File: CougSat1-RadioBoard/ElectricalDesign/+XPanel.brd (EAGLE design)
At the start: 79 x 90 mm, 64 parts, among them J1 ADCS Connector, J2 Low Gain +, J3 Low Gain -, J4 Low Gain Coax, J5 GPS Coax, J6 EPS Connector, U1 AD8515, U3 AD7291

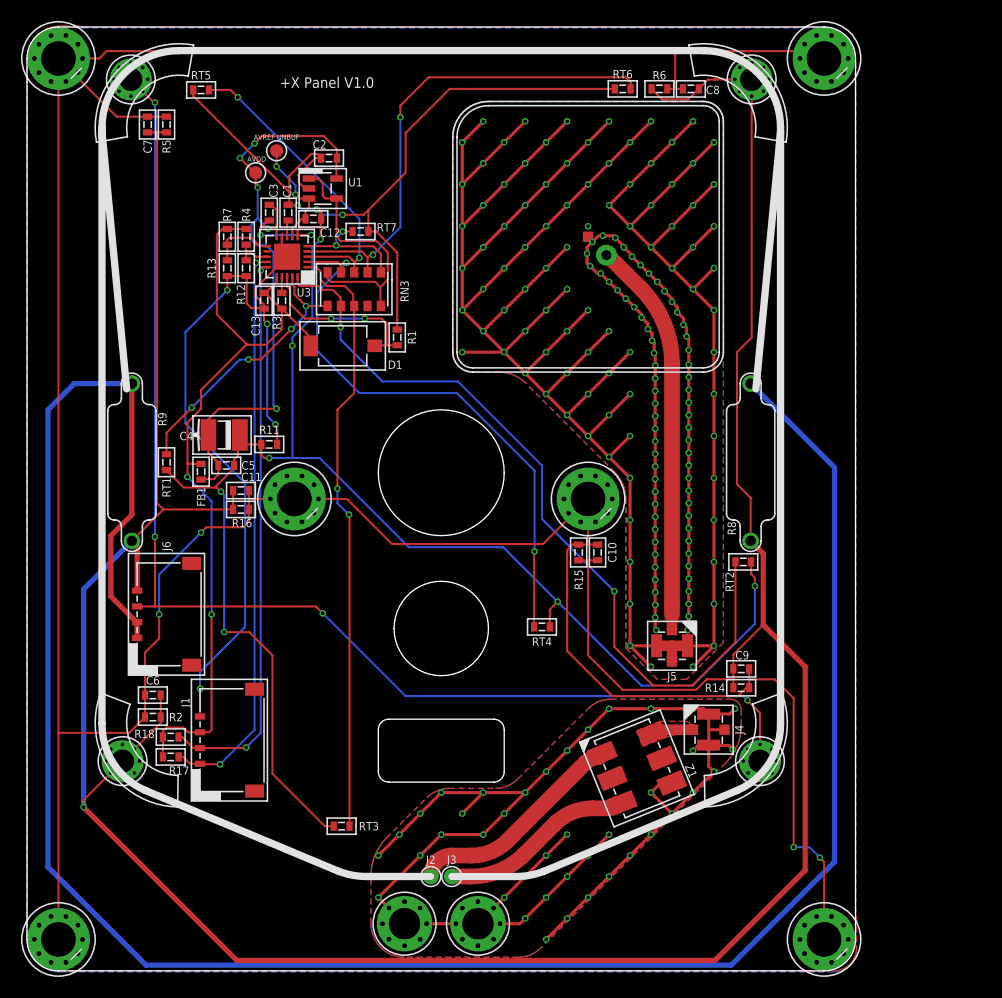
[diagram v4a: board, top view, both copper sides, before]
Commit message: Created mCAD and updated board reference designators and RF soldermask
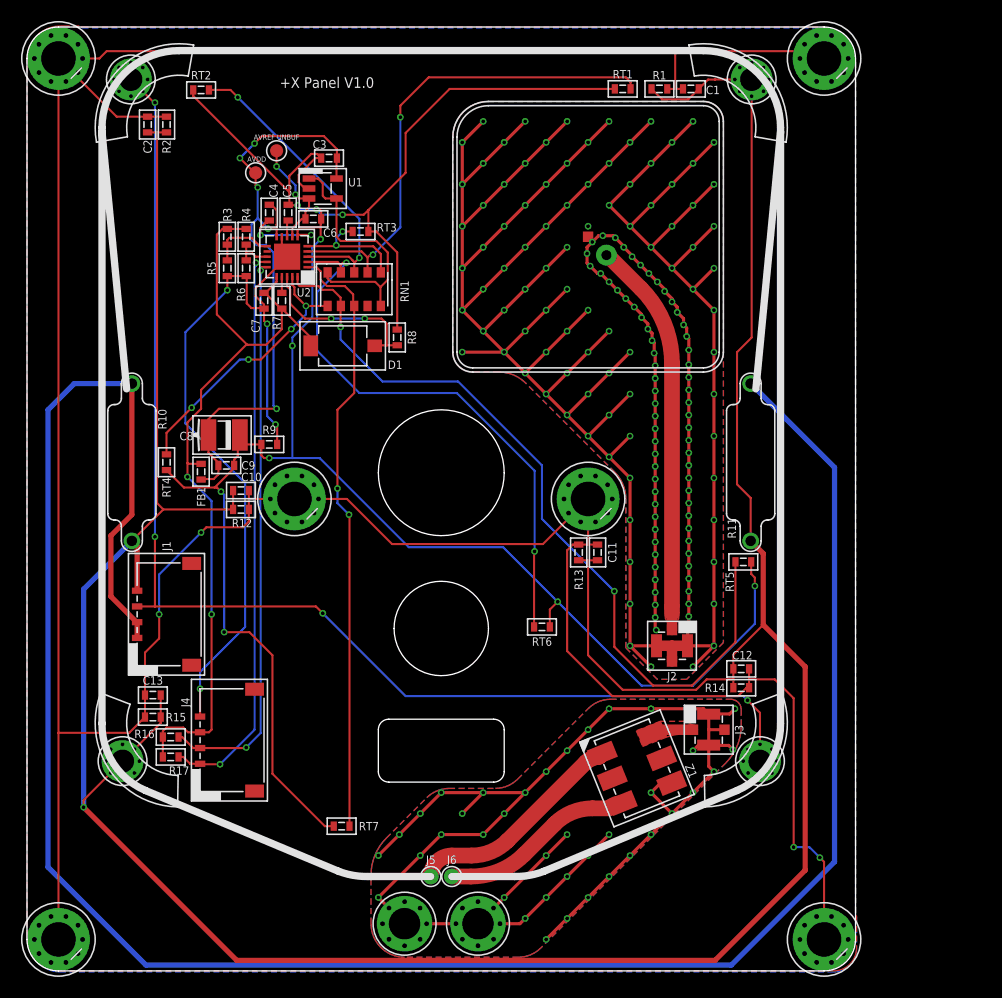
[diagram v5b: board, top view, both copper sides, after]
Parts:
- removed R18: 10kΩ 0.1%, CougsInSpace-Resistors:1608
- added R10: 15Ω 5%, CougsInSpace-Resistors:THT-15MM
- C1: value 1µF 10% -> 100nF 10%
- C12: value 10µF 10% -> 100nF 10%
- C4: value 4.7µF 10% -> 100nF 10%; device CougsInSpace-Capacitors:4028-POL -> CougsInSpace-Capacitors:1608
- C5: value 100nF 10% -> 1µF 10%
- C6: value 100nF 10% -> 10µF 10%
- C8: value 100nF 10% -> 4.7µF 10%; device CougsInSpace-Capacitors:1608 -> CougsInSpace-Capacitors:4028-POL
- H1, H2: value M2 -> M3; device CougsInSpace-Hardware:MOUNTING_HOLE-2.2 -> CougsInSpace-Hardware:MOUNTING_HOLE-3.3
- H10, H9: value M3 -> M2 Nut - 1mm; device CougsInSpace-Hardware:MOUNTING_HOLE-3.3 -> CougsInSpace-Hardware:MOUNTING_HOLE-M2_NUT
- H11, H12: value M2 Nut - 1mm -> M3; device CougsInSpace-Hardware:MOUNTING_HOLE-M2_NUT -> CougsInSpace-Hardware:MOUNTING_HOLE-3.3
- H7, H8: value M3 -> M2; device CougsInSpace-Hardware:MOUNTING_HOLE-3.3 -> CougsInSpace-Hardware:MOUNTING_HOLE-2.2
- J1: value ADCS Connector -> EPS Connector
- J2: value Low Gain + -> GPS Coax; device CougsInSpace-Connectors:THT-0.7 -> CougsInSpace-Connectors:U.FL
- J3: value Low Gain - -> Low Gain Coax; device CougsInSpace-Connectors:THT-0.7 -> CougsInSpace-Connectors:U.FL
- J4: value Low Gain Coax -> ADCS Connector; device CougsInSpace-Connectors:U.FL -> CougsInSpace-Connectors:PICOLOCK1.5-04
- J5: value GPS Coax -> Low Gain +; device CougsInSpace-Connectors:U.FL -> CougsInSpace-Connectors:THT-0.7
- J6: value EPS Connector -> Low Gain -; device CougsInSpace-Connectors:PICOLOCK1.5-04 -> CougsInSpace-Connectors:THT-0.7
- R1: value 2kΩ 0.1% -> 0Ω <20mΩ
- R11: value 0Ω <20mΩ -> 15Ω 5%; device CougsInSpace-Resistors:1608 -> CougsInSpace-Resistors:THT-15MM
- R16: value 0Ω <20mΩ -> 10kΩ 0.1%
- R3: value 1kΩ 0.1% -> 0Ω <20mΩ
- R7: value 0Ω <20mΩ -> 1kΩ 0.1%
- R8: value 15Ω 5% -> 2kΩ 0.1%; device CougsInSpace-Resistors:THT-15MM -> CougsInSpace-Resistors:1608
- R9: value 15Ω 5% -> 0Ω <20mΩ; device CougsInSpace-Resistors:THT-15MM -> CougsInSpace-Resistors:1608
- moved H1 94.7 mm to (-36.5, 42.0)
- moved H7 94.7 mm to (-30.4, -25.0)
- moved RT2 68.5 mm to (-22.9, 39.0), turned to 0 degrees
- moved RT5 68.5 mm to (28.8, -6.00), turned to 180 degrees
- moved H2 66.1 mm to (36.5, 42.0)
- moved H6 65.7 mm to (14.0, 0.00)
- moved H3 65.0 mm to (-29.6, 40.0)
- moved C12 59.2 mm to (28.6, -16.2), turned to 180 degrees
- moved RT3 56.7 mm to (-7.70, 25.5), turned to 180 degrees
- moved RT7 56.7 mm to (-9.50, -31.2), turned to 0 degrees
- moved R2 56.5 mm to (-26.2, 35.7), turned to 90 degrees
- moved RT1 56.2 mm to (17.3, 39.1), turned to 0 degrees
- moved C8 55.4 mm to (-20.7, 6.10), turned to 180 degrees
- moved C9 52.8 mm to (-20.5, 3.20), turned to 0 degrees
- moved RT6 51.9 mm to (9.60, -12.2), turned to 180 degrees
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- renumbered RN3 to RN1, U3 to U2
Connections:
- net 3.3V: now also C7.1, J4.3, R16.2; no longer C13.1, J1.3, R18.2
- net ADC_AS0: now also R3.1, R5.2; no longer R13.2, R7.1
- net ADC_AS1: now also R6.2; no longer R12.2
- net AGND: now also C4.2, C6.2, C8.C, C9.2, R8.1, R9.1; no longer C1.2, C12.2, C2.2, C4.C, R1.1, R11.1
- net AVDD: now also C4.1, C8.A, C9.1; no longer C2.1, C4.A, C5.1
- net AVREF_UNBUF: now also C6.1; no longer C12.1
- net CHASSIS: now also C1.1, C12.1, C13.1, C2.1, H1.1, H1.V1, H1.V10, H1.V2, H1.V3, H1.V4, H1.V5, H1.V6, H1.V7, H1.V8, H1.V9, H11.1, H11.V1, H11.V10, H11.V2, H11.V3, H11.V4, H11.V5, H11.V6, H11.V7, H11.V8, H11.V9, H12.1, H12.V1, H12.V10, H12.V2, H12.V3, H12.V4, H12.V5, H12.V6, H12.V7, H12.V8, H12.V9, H2.1, H2.V1, H2.V10, H2.V2, H2.V3, H2.V4, H2.V5, H2.V6, H2.V7, H2.V8, H2.V9, R1.2, R12.2, R13.2; no longer C6.1, C7.1, C8.1, C9.1, H10.1, H10.V1, H10.V10, H10.V2, H10.V3, H10.V4, H10.V5, H10.V6, H10.V7, H10.V8, H10.V9, H7.1, H7.V1, H7.V10, H7.V2, H7.V3, H7.V4, H7.V5, H7.V6, H7.V7, H7.V8, H7.V9, H8.1, H8.V1, H8.V10, H8.V2, H8.V3, H8.V4, H8.V5, H8.V6, H8.V7, H8.V8, H8.V9, H9.1, H9.V1, H9.V10, H9.V2, H9.V3, H9.V4, H9.V5, H9.V6, H9.V7, H9.V8, H9.V9, R16.2, R5.2, R6.2
- net DCAP: now also C5.1; no longer C1.1
- net DGND: now also C7.2, J4.4, R5.1, R6.1, R9.2; no longer C13.2, J1.4, R11.2, R12.1, R13.1
- net GPS_COAX: now also J2.CENTER; no longer J5.CENTER
- net I2C_SCL_ADCS: now also J4.2, R16.1; no longer J1.2, R18.1
- net I2C_SDA_ADCS: now also J4.1; no longer J1.1
- net LOW_GAIN_COAX: now also J3.CENTER; no longer J4.CENTER
- net LOW_GAIN_N: now also J6.1; no longer J3.1
- net LOW_GAIN_P: now also J5.1; no longer J2.1
- net PD_RST: now also R7.1; no longer R3.1
- net PGND: now also C1.2, C12.2, C13.2, C2.2, H7.1, H7.V1, H7.V2, H7.V3, H7.V4, H7.V5, H7.V6, H7.V7, H7.V8, J1.4, R1.1, R10.1, R11.1, R12.1, R13.1; no longer C6.2, C7.2, C8.2, C9.2, H3.1, H3.V1, H3.V2, H3.V3, H3.V4, H3.V5, H3.V6, H3.V7, H3.V8, J6.4, R16.1, R5.1, R6.1, R8.1, R9.1
- net PHOTO: now also R8.2; no longer R1.2
- net RFGND-0: now also H10.1, H10.V1, H10.V2, H10.V3, H10.V4, H10.V5, H10.V6, H10.V7, H10.V8, H9.1, H9.V1, H9.V2, H9.V3, H9.V4, H9.V5, H9.V6, H9.V7, H9.V8, J3.SHIELD@1, J3.SHIELD@13, J3.SHIELD@2; no longer H11.1, H11.V1, H11.V2, H11.V3, H11.V4, H11.V5, H11.V6, H11.V7, H11.V8, H12.1, H12.V1, H12.V2, H12.V3, H12.V4, H12.V5, H12.V6, H12.V7, H12.V8, J4.SHIELD@1, J4.SHIELD@13, J4.SHIELD@2
- net RFGND-1: now also J2.SHIELD@1, J2.SHIELD@13, J2.SHIELD@2; no longer J5.SHIELD@1, J5.SHIELD@13, J5.SHIELD@2
- net SENSE: now also H3.1, H3.V1, H3.V2, H3.V3, H3.V4, H3.V5, H3.V6, H3.V7, H3.V8, H8.1, H8.V1, H8.V2, H8.V3, H8.V4, H8.V5, H8.V6, H8.V7, H8.V8, J1.3; no longer H1.1, H1.V1, H1.V2, H1.V3, H1.V4, H1.V5, H1.V6, H1.V7, H1.V8, H2.1, H2.V1, H2.V2, H2.V3, H2.V4, H2.V5, H2.V6, H2.V7, H2.V8, J6.3
- net THERM-0: now also RT4.2; no longer RT1.2
- net THERM-1: now also RT5.2; no longer RT2.2
- net THERM-2: now also RT7.2; no longer RT3.2
- net THERM-3: now also RT6.2; no longer RT4.2
- net THERM-4: now also RT2.2; no longer RT5.2
- net THERM-5: now also RT1.2; no longer RT6.2
- net THERM-6: now also RT3.2; no longer RT7.2
- net VCC: now also J1.1, J1.2, R10.2, R11.2; no longer J6.1, J6.2, R8.2, R9.2
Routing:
- net CHASSIS: track 457.7 -> 456.6 mm

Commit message: Photodiode Test
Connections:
- net VCC renamed DEPLOYABLE
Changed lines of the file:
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@@
 <?xml version="1.0" encoding="utf-8"?>
 <!DOCTYPE eagle SYSTEM "eagle.dtd">
-<eagle version="9.5.1">
+<eagle version="9.5.2">
 <drawing>
 <settings>
-<setting alwaysvectorfont="yes"/>
+<setting alwaysvectorfont="no"/>
 <setting verticaltext="up"/>
 </settings>
@@
 </polygon>
 </signal>
-<signal name="VCC">
+<signal name="DEPLOYABLE">
 <contactref element="J1" pad="1"/>
 <contactref element="R11" pad="2"/>

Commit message: Changed resistors
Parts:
- R10, R11: value 15Ω 5% -> 5Ω 1%
- moved R11 16.9 mm to (42.9, -6.80), turned to 0 degrees
- moved R2 7.85 mm to (-22.1, 29.0)
- moved C2 7.77 mm to (-23.9, 29.1)
- moved RT2 6.45 mm to (-22.1, 32.6)
- moved R10 0.78 mm to (-29.0, 2.90)
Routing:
- net DEPLOYABLE: track 210.6 -> 25.8 mm
- net PGND: track 324.6 -> 307.1 mm
- net CHASSIS: track 456.6 -> 463.4 mm
- net THERM-4: track 29.5 -> 33.0 mm
- net AGND: track 234.0 -> 231.2 mm
- net SENSE: track 144.5 -> 146.6 mm

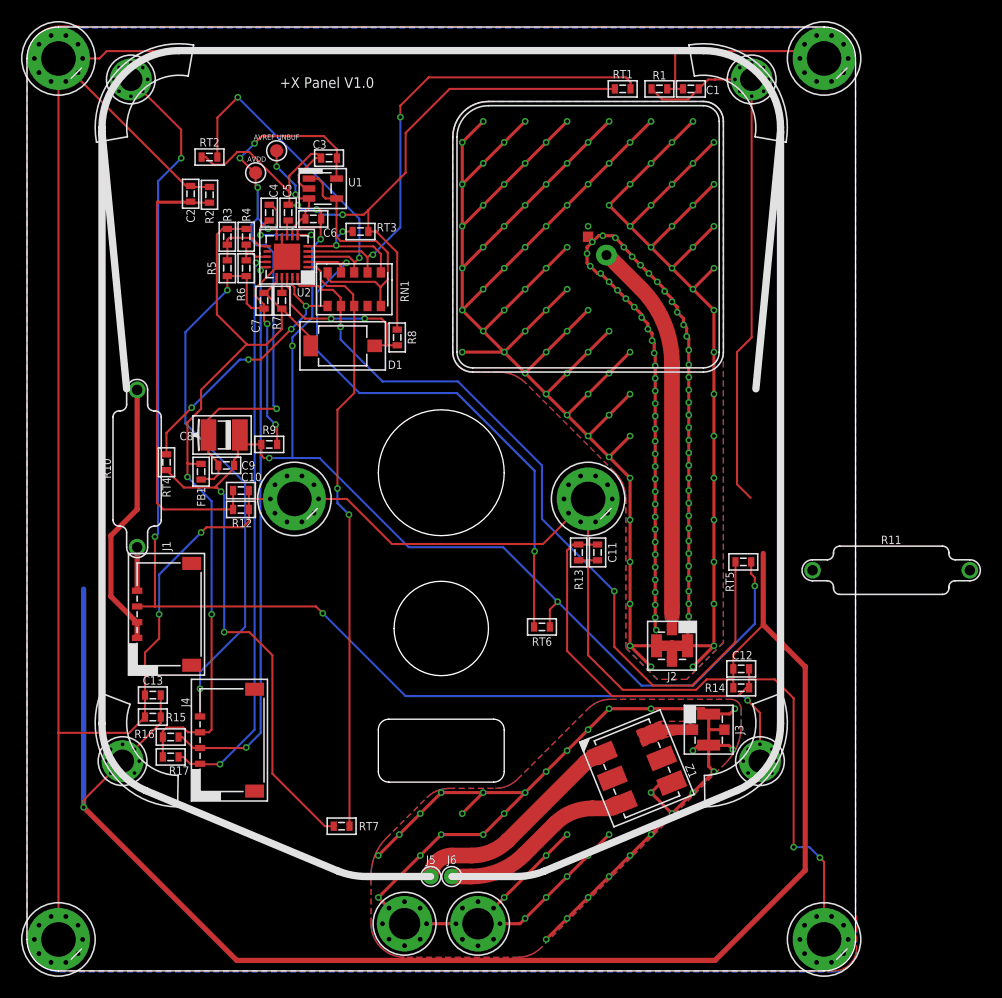
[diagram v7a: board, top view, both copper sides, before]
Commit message: Placed critical location components
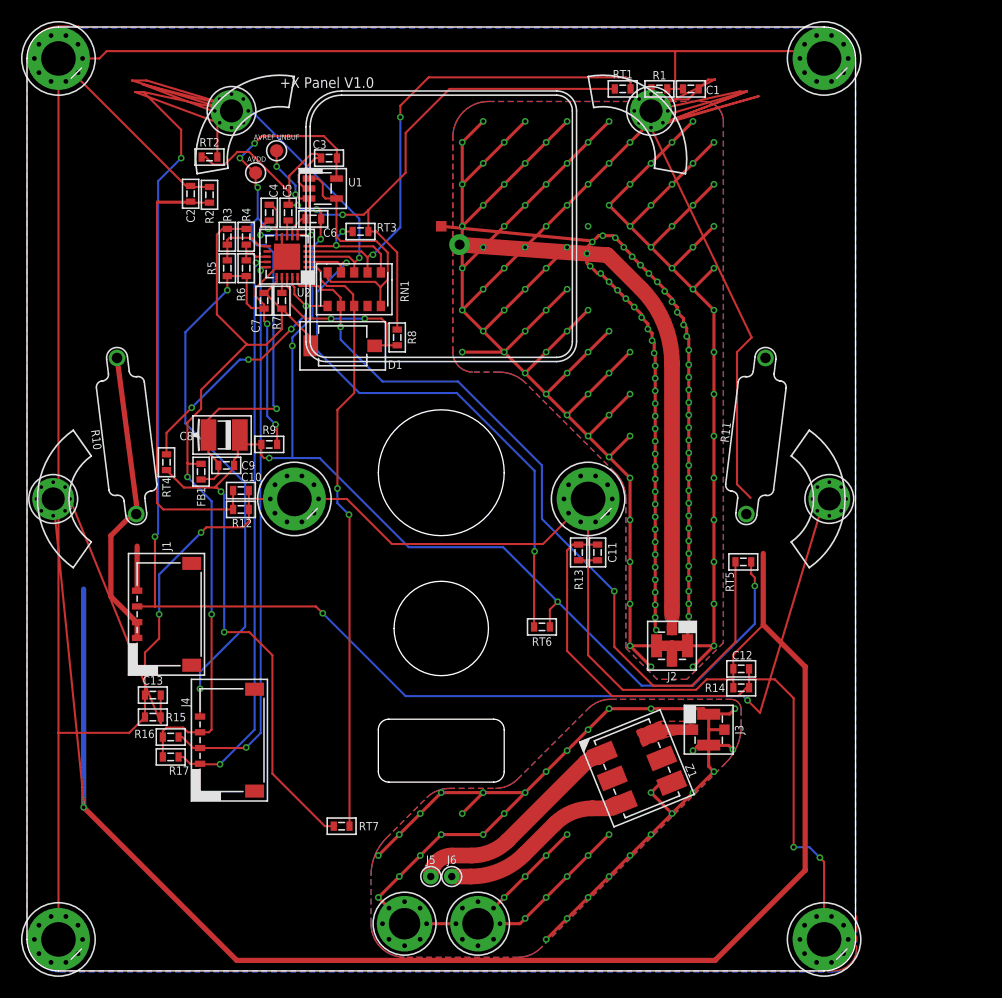
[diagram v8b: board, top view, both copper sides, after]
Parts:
- moved H7 25.9 mm to (-37.0, 0.00)
- moved H8 25.9 mm to (37.0, 0.00)
- moved R11 18.2 mm to (30.0, 6.00), turned to 83 degrees
- moved AE1 14.0 mm to (0.00, 26.0)
- moved H3 10.1 mm to (-20.0, 37.0)
- moved H4 10.1 mm to (20.0, 37.0)
- moved R10 3.26 mm to (-30.0, 6.00), turned to 97 degrees
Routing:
- net PGND: track 307.1 -> 408.1 mm
- net SENSE: track 146.6 -> 221.8 mm
- net GPS_COAX: track 37.8 -> 51.8 mm
- net RFGND-1: track 369.1 -> 383.0 mm
- net DEPLOYABLE: track 25.8 -> 28.9 mm
- net THERM-4: vias 2 -> 1
